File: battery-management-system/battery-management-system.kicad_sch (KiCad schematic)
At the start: 4 parts

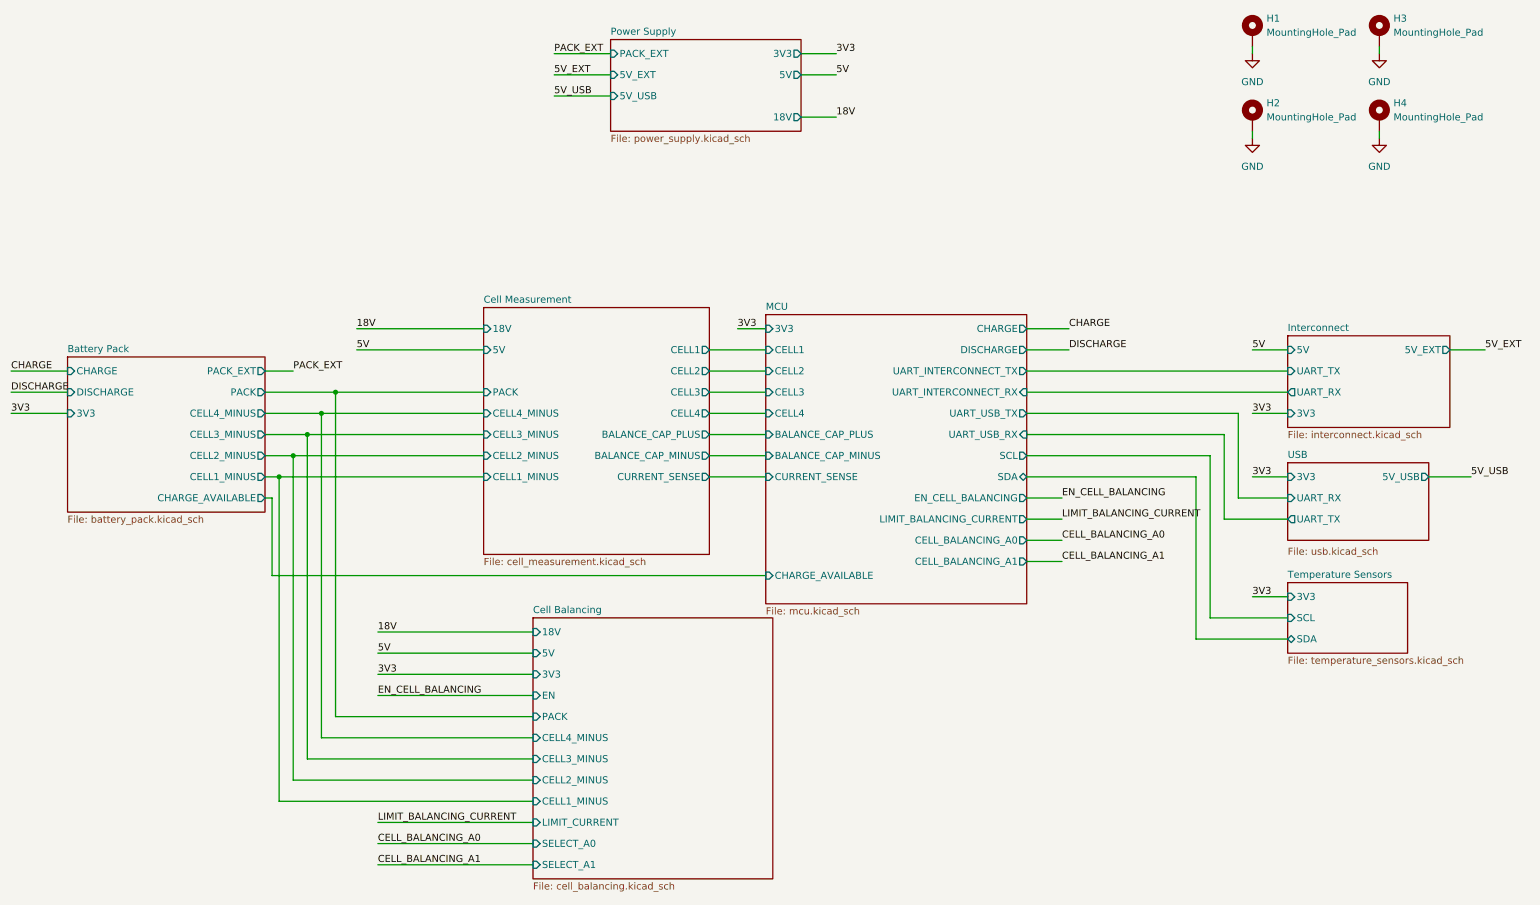
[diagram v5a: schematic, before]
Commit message: finish cell balancing changes
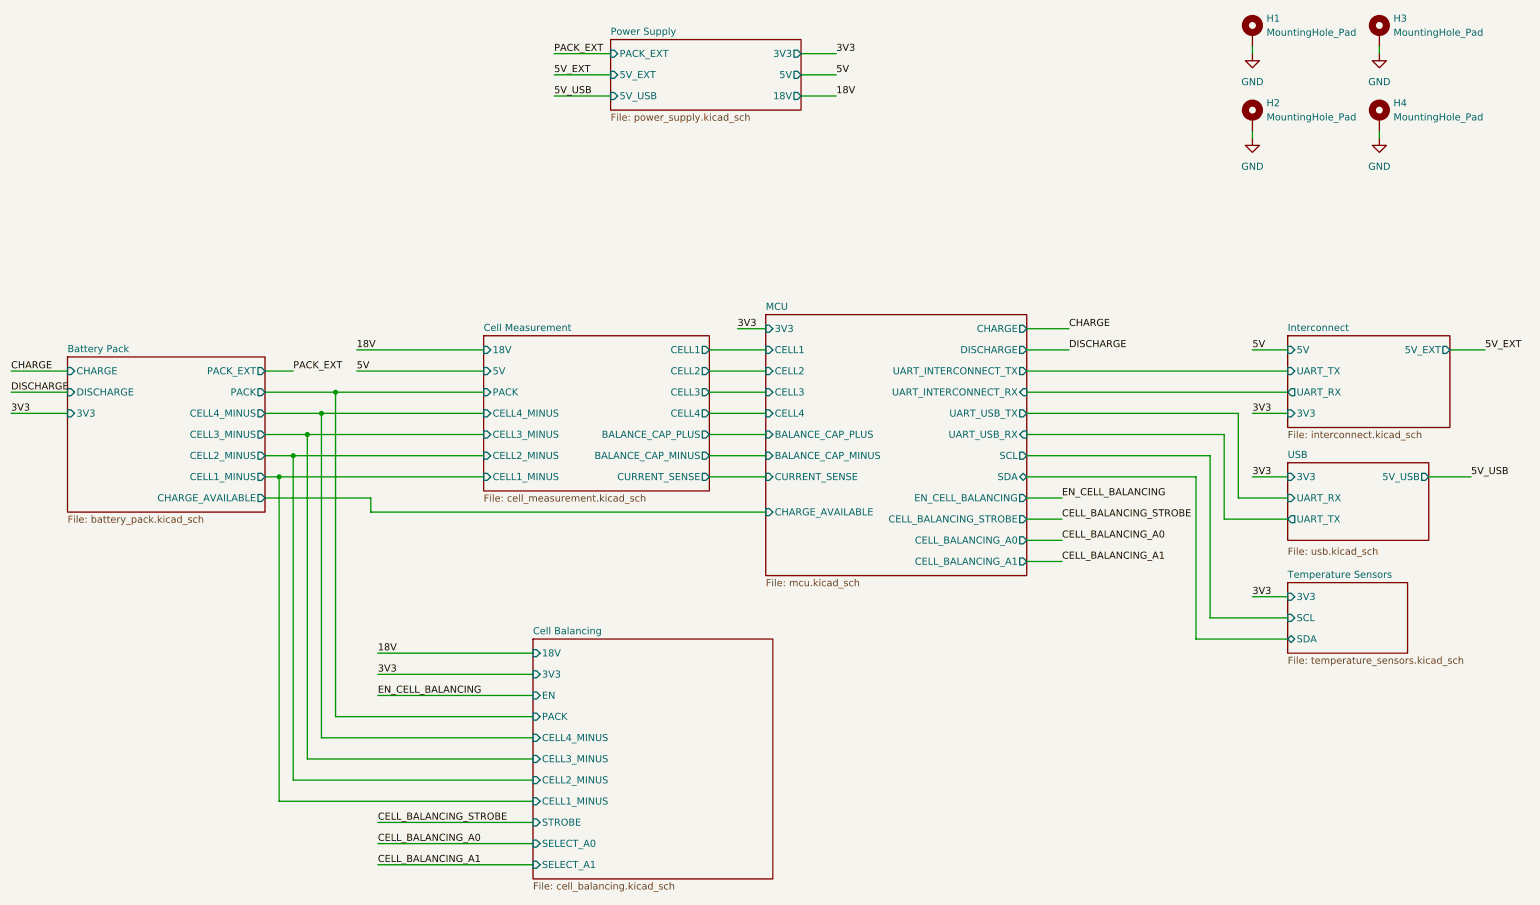
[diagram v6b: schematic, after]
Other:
- sheet Cell Balancing ports: added STROBE; removed 5V, LIMIT_CURRENT
- sheet MCU ports: added CELL_BALANCING_STROBE; removed LIMIT_BALANCING_CURRENT

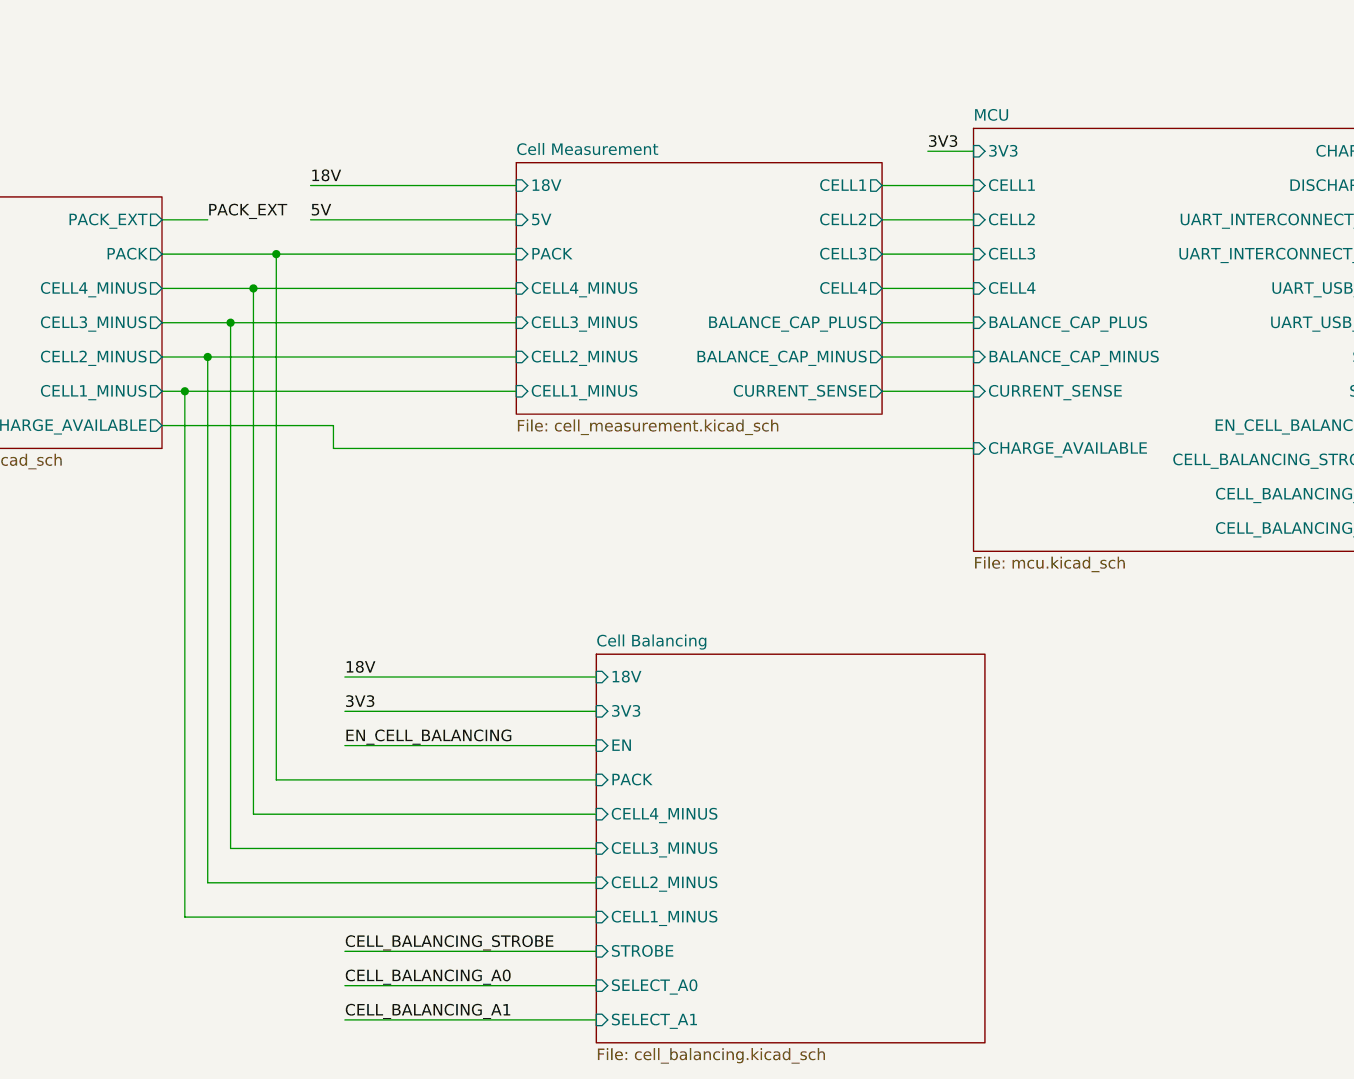
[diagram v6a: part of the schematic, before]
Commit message: fix electrical rule check errors
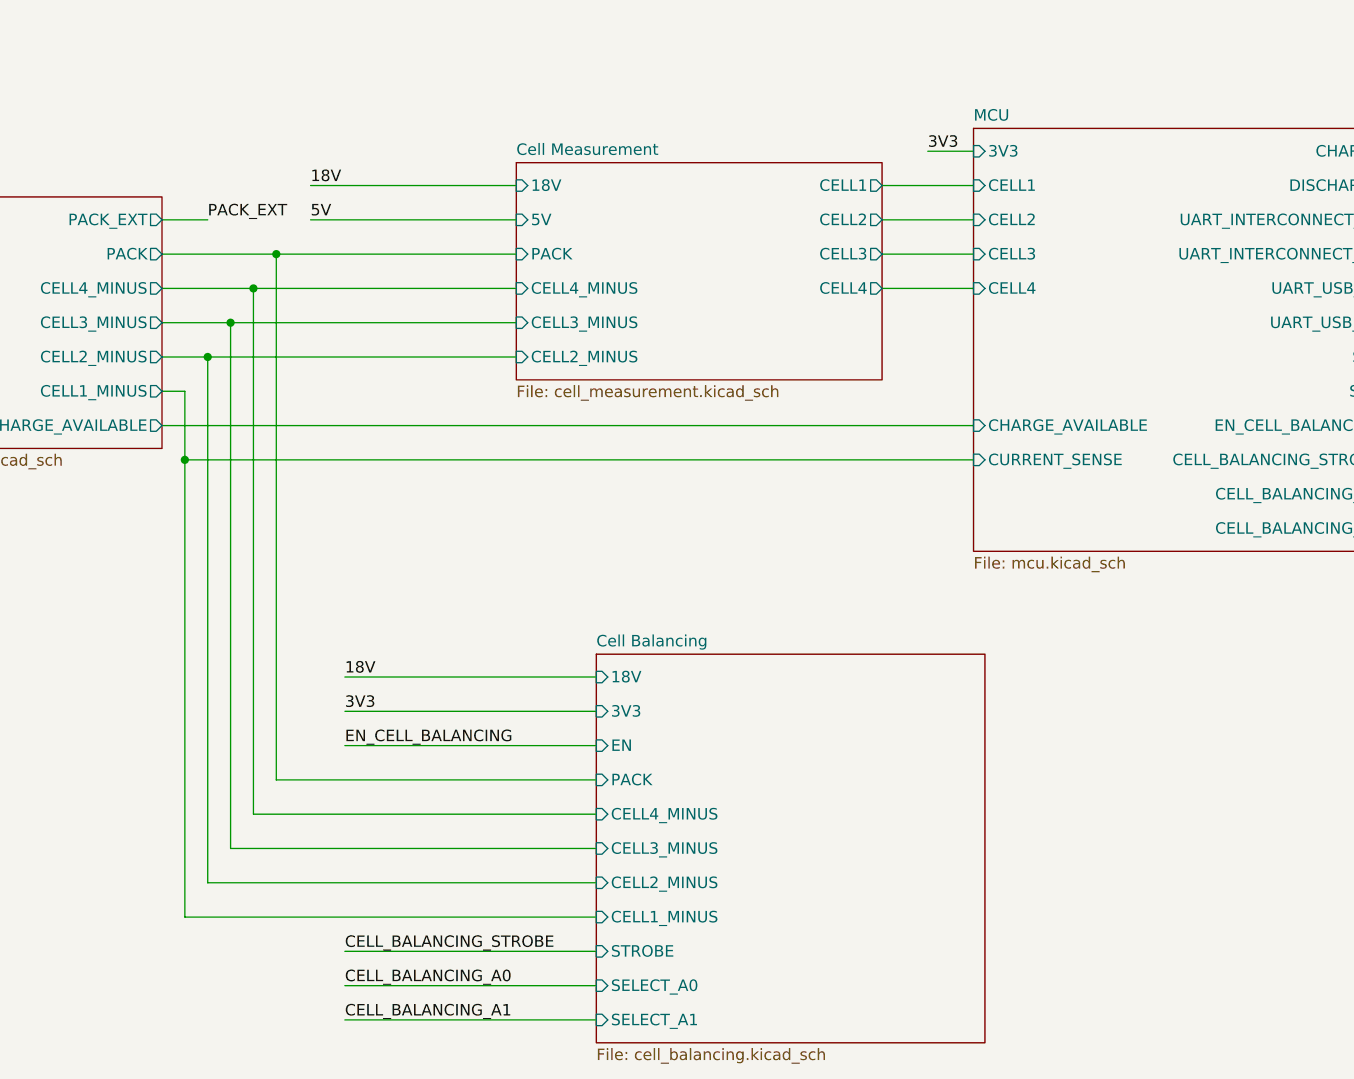
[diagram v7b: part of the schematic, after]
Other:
- sheet Cell Measurement ports: added none; removed BALANCE_CAP_MINUS, BALANCE_CAP_PLUS, CELL1_MINUS, CURRENT_SENSE
- sheet MCU ports: added none; removed BALANCE_CAP_MINUS, BALANCE_CAP_PLUS
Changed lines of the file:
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@@
 (kicad_sch (version 20230121) (generator eeschema)
   (paper "A4")
-  (junction (at 60.96 102.87) (diameter 0) (color 0 0 0 0)
-  )
   (junction (at 66.04 95.25) (diameter 0) (color 0 0 0 0)
   )
   (junction (at 63.5 99.06) (diameter 0) (color 0 0 0 0)
   )
+  (junction (at 60.96 110.49) (diameter 0) (color 0 0 0 0)
+  )
   (junction (at 71.12 87.63) (diameter 0) (color 0 0 0 0)
   )
@@
     (stroke (width 0) (type default))
   )
-  (wire (pts (xy 77.47 109.22) (xy 148.59 109.22))
+  (wire (pts (xy 58.42 106.68) (xy 148.59 106.68))
     (stroke (width 0) (type default))
   )
@@
     (stroke (width 0) (type default))
   )
-  (wire (pts (xy 60.96 102.87) (xy 60.96 161.29))
+  (wire (pts (xy 60.96 102.87) (xy 60.96 110.49))
+    (stroke (width 0) (type default))
+  )
+  (wire (pts (xy 60.96 110.49) (xy 148.59 110.49))
+    (stroke (width 0) (type default))
+  )
+  (wire (pts (xy 60.96 110.49) (xy 60.96 161.29))
     (stroke (width 0) (type default))
   )
@@
     (stroke (width 0) (type default))
   )
-  (wire (pts (xy 138.43 95.25) (xy 148.59 95.25))
-    (stroke (width 0) (type default))
-  )
   (wire (pts (xy 228.6 99.06) (xy 228.6 128.27))
     (stroke (width 0) (type default))
@@
     (stroke (width 0) (type default))
   )
-  (wire (pts (xy 138.43 99.06) (xy 148.59 99.06))
-    (stroke (width 0) (type default))
-  )
   (wire (pts (xy 12.7 87.63) (xy 22.86 87.63))
     (stroke (width 0) (type default))
@@
     (stroke (width 0) (type default))
   )
-  (wire (pts (xy 138.43 102.87) (xy 148.59 102.87))
-    (stroke (width 0) (type default))
-  )
   (wire (pts (xy 154.94 26.67) (xy 161.29 26.67))
     (stroke (width 0) (type default))
@@
     (stroke (width 0) (type default))
   )
-  (wire (pts (xy 58.42 106.68) (xy 77.47 106.68))
-    (stroke (width 0) (type default))
-  )
   (wire (pts (xy 138.43 80.01) (xy 148.59 80.01))
     (stroke (width 0) (type default))
@@
     (stroke (width 0) (type default))
   )
-  (wire (pts (xy 60.96 102.87) (xy 97.79 102.87))
-    (stroke (width 0) (type default))
-  )
   (wire (pts (xy 236.22 91.44) (xy 242.57 91.44))
     (stroke (width 0) (type default))
@@
   )
   (wire (pts (xy 143.51 76.2) (xy 148.59 76.2))
-    (stroke (width 0) (type default))
-  )
-  (wire (pts (xy 77.47 109.22) (xy 77.47 106.68))
     (stroke (width 0) (type default))
   )
@@
     )
   )
-  (sheet (at 97.79 77.47) (size 40.64 27.94) (fields_autoplaced)
+  (sheet (at 97.79 77.47) (size 40.64 24.13) (fields_autoplaced)
     (stroke (width 0.1524) (type solid))
     (fill (color 0 0 0 0.0000))
@@
       (effects (font (size 1.27 1.27)) (justify left bottom))
     )
-    (property "Sheetfile" "cell_measurement.kicad_sch" (at 97.79 105.9946 0)
+    (property "Sheetfile" "cell_measurement.kicad_sch" (at 97.79 102.1846 0)
       (effects (font (size 1.27 1.27)) (justify left top))
     )
@@
     (pin "CELL4" output (at 138.43 91.44 0)
       (effects (font (size 1.27 1.27)) (justify right))
-    )
-    (pin "BALANCE_CAP_PLUS" output (at 138.43 95.25 0)
-      (effects (font (size 1.27 1.27)) (justify right))
-    )
-    (pin "BALANCE_CAP_MINUS" output (at 138.43 99.06 0)
-      (effects (font (size 1.27 1.27)) (justify right))
-    )
-    (pin "CURRENT_SENSE" output (at 138.43 102.87 0)
-      (effects (font (size 1.27 1.27)) (justify right))
-    )
-    (pin "CELL1_MINUS" input (at 97.79 102.87 180)
-      (effects (font (size 1.27 1.27)) (justify left))
     )
     (pin "5V" input (at 97.79 83.82 180)
@@
       (effects (font (size 1.27 1.27)) (justify right))
     )
-    (pin "BALANCE_CAP_PLUS" input (at 148.59 95.25 180)
-      (effects (font (size 1.27 1.27)) (justify left))
-    )
-    (pin "BALANCE_CAP_MINUS" input (at 148.59 99.06 180)
-      (effects (font (size 1.27 1.27)) (justify left))
-    )
     (pin "SDA" bidirectional (at 195.58 102.87 0)
       (effects (font (size 1.27 1.27)) (justify right))
@@
       (effects (font (size 1.27 1.27)) (justify right))
     )
-    (pin "CHARGE_AVAILABLE" input (at 148.59 109.22 180)
-      (effects (font (size 1.27 1.27)) (justify left))
-    )
-    (pin "CURRENT_SENSE" input (at 148.59 102.87 180)
-      (effects (font (size 1.27 1.27)) (justify left))
-    )
+    (pin "CHARGE_AVAILABLE" input (at 148.59 106.68 180)
+      (effects (font (size 1.27 1.27)) (justify left))
+    )
+    (pin "CURRENT_SENSE" input (at 148.59 110.49 180)
+      (effects (font (size 1.27 1.27)) (justify left))
+    )
